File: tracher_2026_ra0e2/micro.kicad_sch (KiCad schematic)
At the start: 30 parts, among them IC1 E22-900M22S, J1 TC2030, J2 RFPC-SMA28-F, U1 R7FA0E2094CFM

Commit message: Change U1 to LQFP-48 for hand-solderable prototypes
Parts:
- U1: footprint Package_QFN:QFN-48-1EP_7x7mm_P0.5mm_EP5.6x5.6mm -> Package_QFP:LQFP-48_7x7mm_P0.5mm
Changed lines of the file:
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@@
 			)
 		)
-		(property "Footprint" "Package_QFN:QFN-48-1EP_7x7mm_P0.5mm_EP5.6x5.6mm"
+		(property "Footprint" "Package_QFP:LQFP-48_7x7mm_P0.5mm"
 			(at 180.34 97.79 0)
 			(hide yes)

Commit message: removed Acc
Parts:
- C10: value 1uF/16V -> 1uF
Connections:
- net at C10.1: no longer U1.3 (VCL)
- net MCU_I2C_SCL: no longer names the net of U1.1 (P400/SCLA1)
- net MCU_I2C_SDA: no longer names the net of U1.2 (P401/SDAA1)
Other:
- moved on the sheet: C10

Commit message: J1 Tag-Connect rewired to standard ARM 6-pin SWD pinout (1=VTRef/+3.3V, 2=SWDIO, 3=nRESET, 4=SWCLK, 5=GND, 6=NC)
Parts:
- C10: value 1uF -> 1uF/16V
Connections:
- net +3.3V: now also J1.1; no longer J1.4
- net GND: now also J1.5; no longer J1.3
- net MCU_RST: now also J1.3; no longer J1.1
- net at C10.1: now also U1.3 (VCL)
- net MCU_I2C_SCL: now reaches U1.1 (P400/SCLA1)
- net MCU_I2C_SDA: now reaches U1.2 (P401/SDAA1)
- net at U1.24 (P300/SWCLK): now also J1.4; no longer J1.6
- net at U1.25 (P108/SWDIO): now also J1.2; no longer J1.5
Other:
- moved on the sheet: C10

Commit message: Cleaned up the schamatic
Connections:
- net +3.3V: now also C11.1; no longer C11.2
- net GND: now also C11.2; no longer C11.1
- net MCU_I2C_SCL: no longer names the net of U1.1 (P400/SCLA1)
- net MCU_I2C_SDA: no longer names the net of U1.2 (P401/SDAA1)
- no-connect marks 18 -> 19
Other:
- moved on the sheet: C10, C11

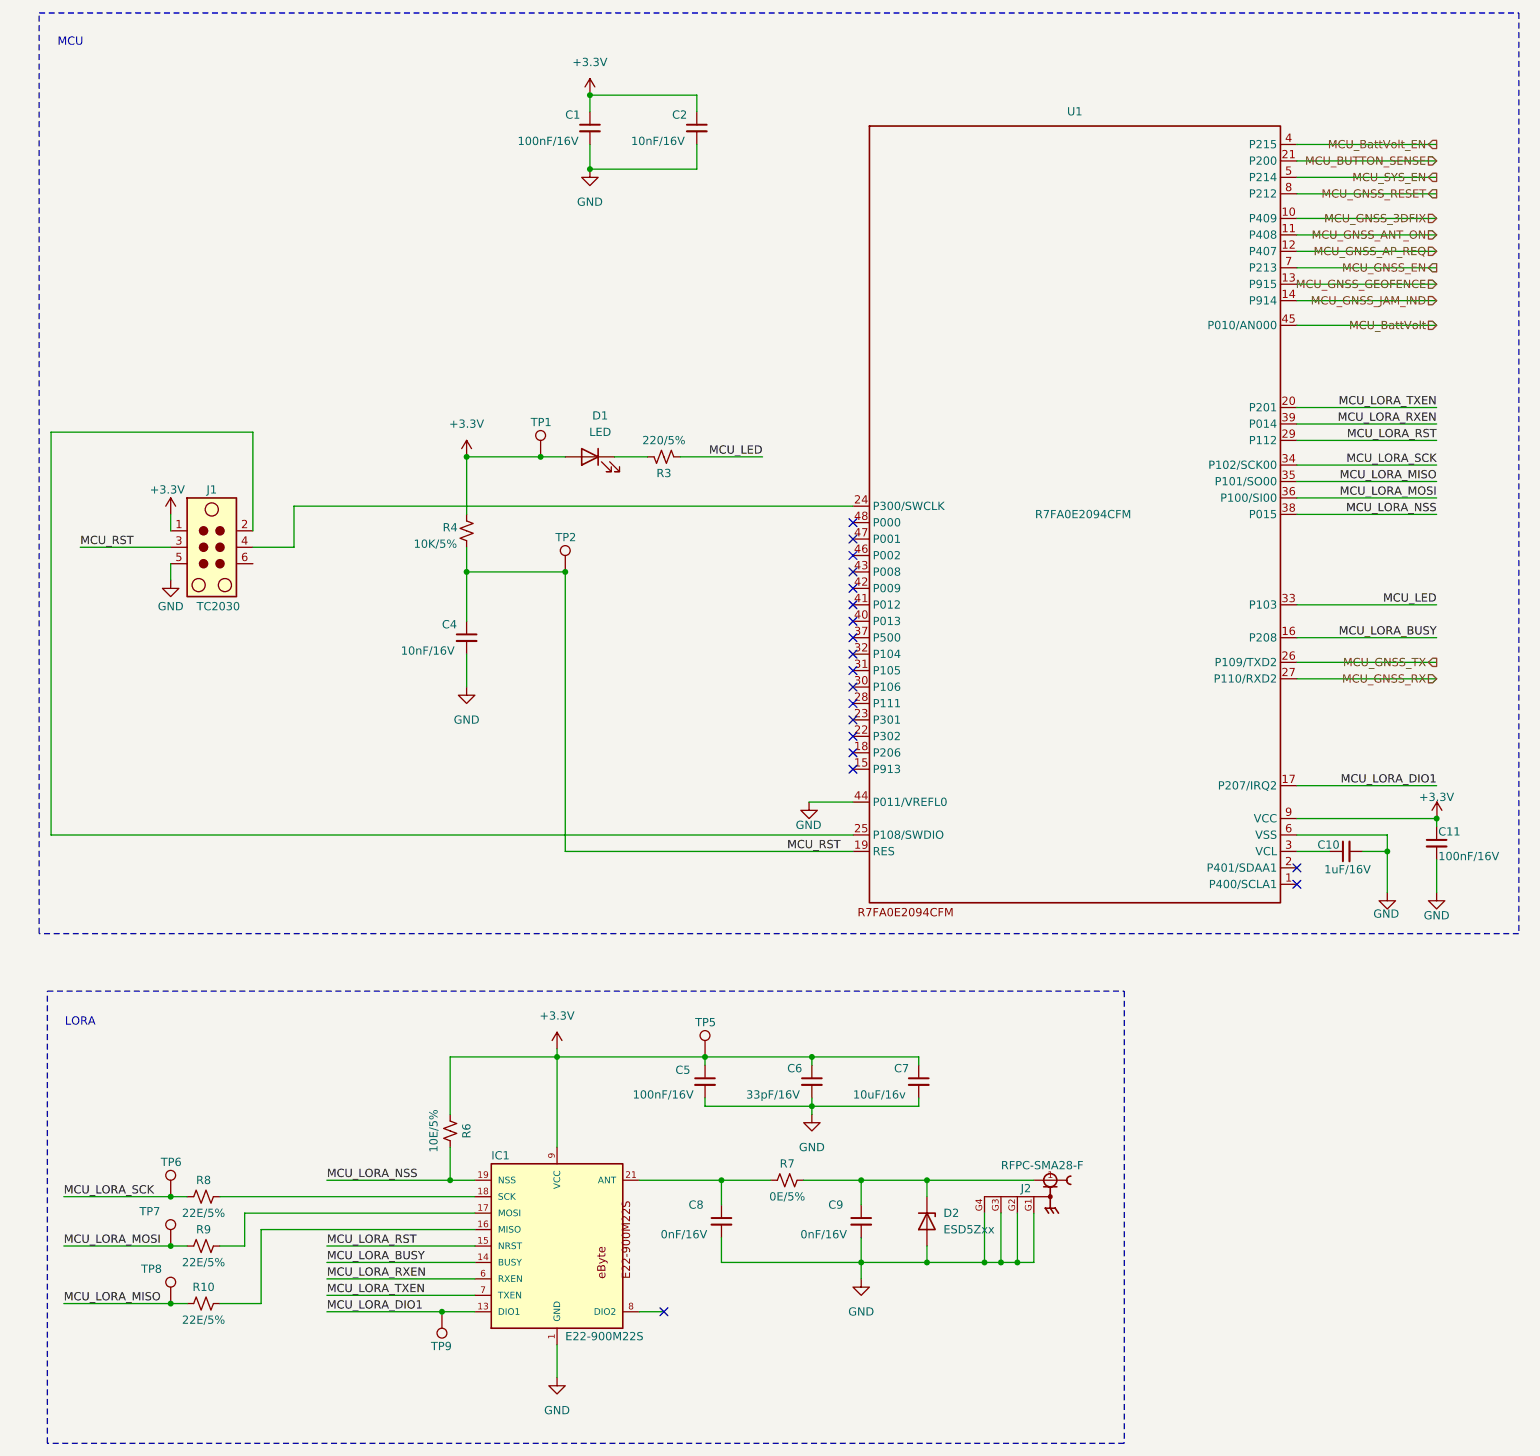
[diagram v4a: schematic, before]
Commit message: 32-pin RA0E2 (R7FA0E2094CFJ): rewrite U1 symbol and rewire schematic
- Replace 48-pin U1 with 32-pin QFN symbol (PawPrint:R7FA0E2094CFJ)
- Rewire all 23 signals per verified 32-pin assignment
- Fix P214/P215 input-only bug: BattVolt_EN->P213, SYS_EN->P212
- Remove cut nets: I2C (U5 gone), ANT_ON, AP_REQ, D_TX
- Fix J1 SWD: remove pin shorts, proper VTRef/GND, SWDIO/SWCLK via labels
- Add PawPrint.kicad_sym library and QFN-32 footprint
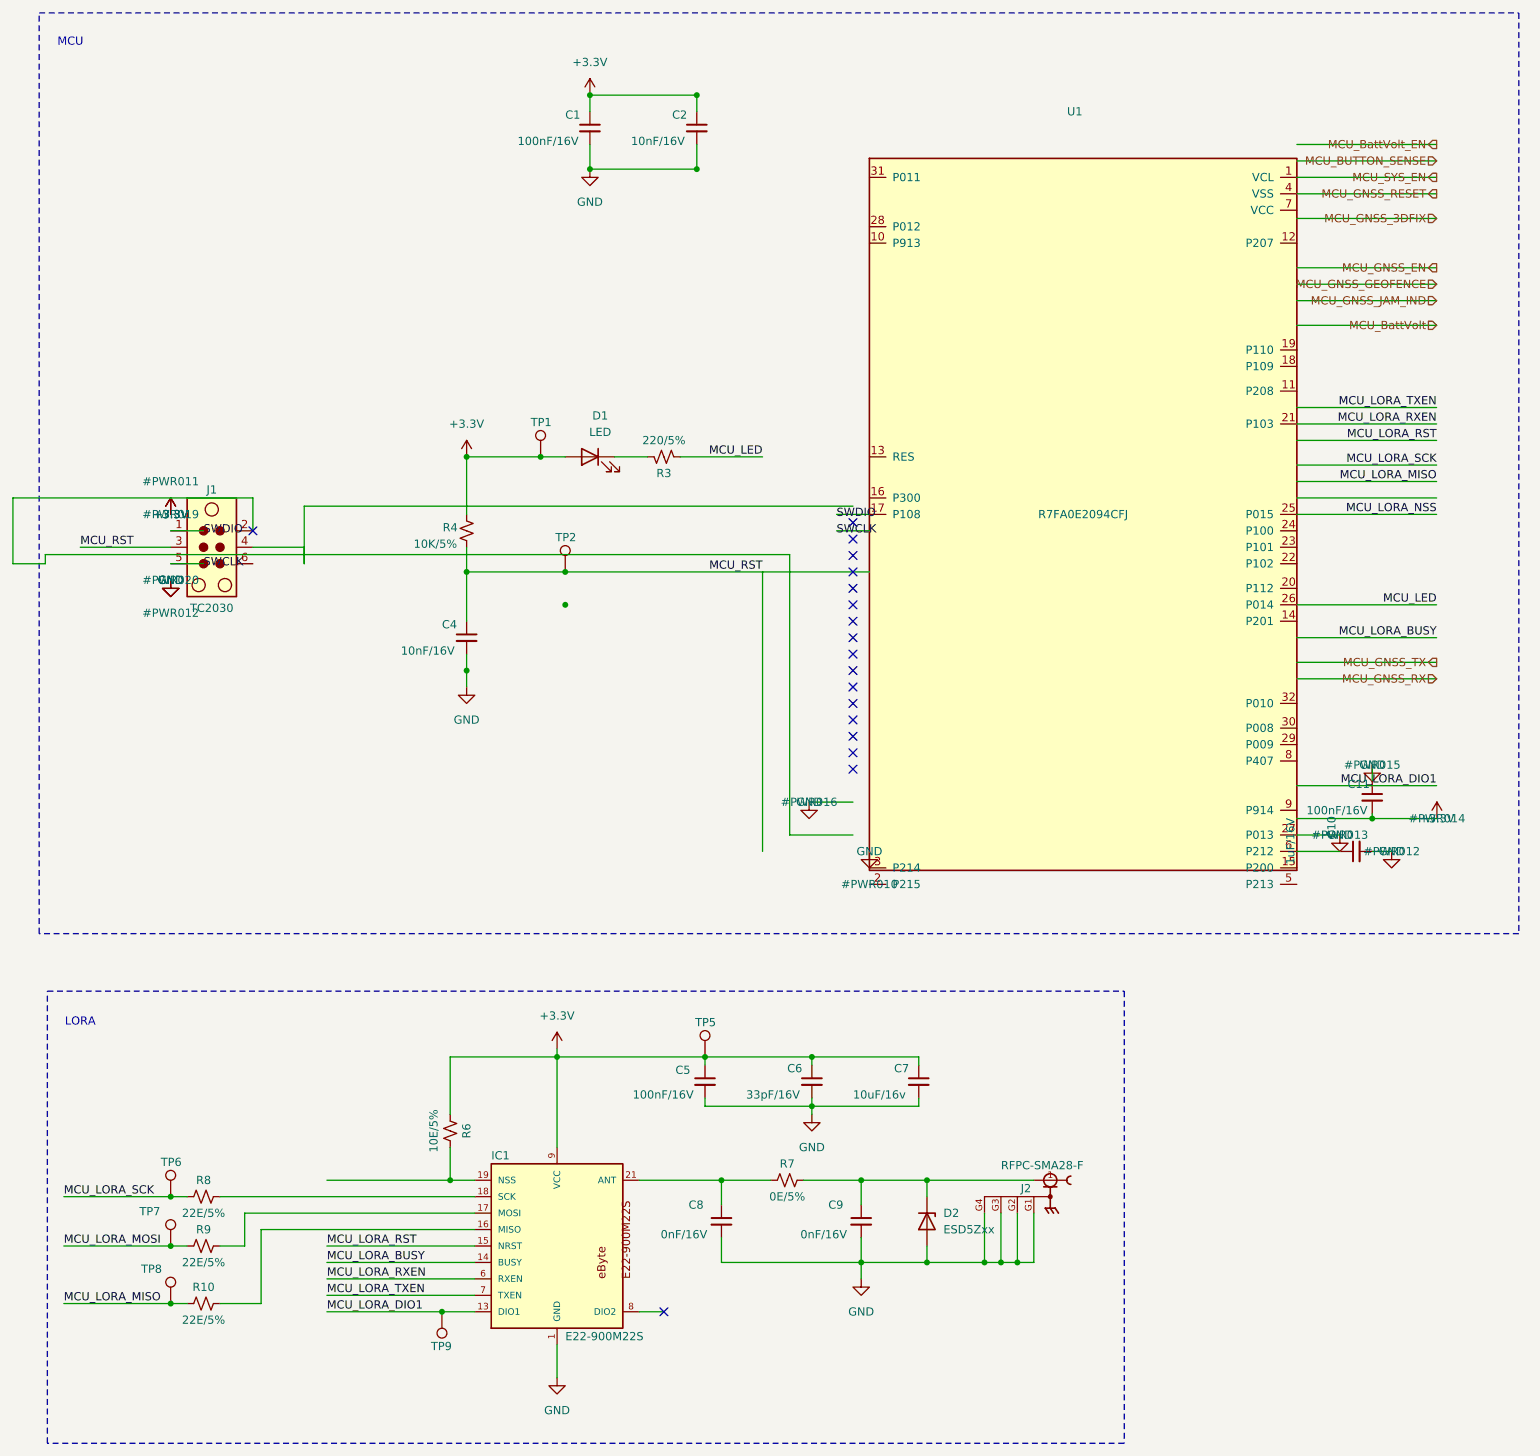
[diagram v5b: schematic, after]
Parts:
- U1: value R7FA0E2094CFM -> R7FA0E2094CFJ; footprint Package_QFP:LQFP-48_7x7mm_P0.5mm -> PawPrint:QFN-32_5x5mm_P0.5mm; symbol Custom:R7FA0E2094CFM -> PawPrint:R7FA0E2094CFJ
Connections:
- net +3.3V: now also C11.2; no longer C11.1, J1.1, U1.9 (VCC)
- net GND: now also C11.1, U1.27 (P013); no longer C11.2, J1.5, U1.44 (P011/VREFL0), U1.6 (VSS)
- net MCU_BUTTON_SENSE: no longer U1.21 (P200)
- net MCU_BattVolt: no longer U1.45 (P010/AN000)
- net MCU_BattVolt_EN: no longer U1.4 (P215)
- net MCU_GNSS_3DFIX: no longer U1.10 (P409)
- net MCU_GNSS_EN: no longer U1.7 (P213)
- net MCU_GNSS_GEOFENCE: no longer U1.13 (P915)
- net MCU_GNSS_JAM_IND: no longer U1.14 (P914)
- net MCU_GNSS_RESET: now also U1.4 (VSS); no longer U1.8 (P212)
- net MCU_GNSS_RX: no longer U1.27 (P110/RXD2)
- net MCU_GNSS_TX: no longer U1.26 (P109/TXD2)
- net MCU_LED: now also U1.26 (P014); no longer U1.33 (P103)
- net MCU_LORA_BUSY: no longer U1.16 (P208)
- net MCU_LORA_DIO1: no longer U1.17 (P207/IRQ2)
- net MCU_LORA_MISO: no longer U1.35 (P101/SO00)
- net MCU_LORA_MOSI: no longer U1.36 (P100/SI00)
- net MCU_LORA_NSS: now also U1.25 (P015); no longer IC1.19 (NSS), R6.1, U1.38 (P015)
- net MCU_LORA_RST: no longer U1.29 (P112)
- net MCU_LORA_RXEN: now also U1.21 (P103); no longer U1.39 (P014)
- net MCU_LORA_SCK: no longer U1.34 (P102/SCK00)
- net MCU_LORA_TXEN: no longer U1.20 (P201)
- net MCU_RST: no longer U1.19 (RES)
- net MCU_SYS_EN: now also U1.1 (VCL); no longer U1.5 (P214)
- net at C10.1: now also U1.6 (P212); no longer U1.3 (VCL)
- net at U1.24 (P100): no longer J1.4
- net at J1.2: no longer U1.25 (P108/SWDIO)
- net MCU_GNSS_ANT_ON: no longer names the net of U1.11 (P208)
- net MCU_GNSS_AP_REQ: no longer names the net of U1.12 (P207)
- new net: IC1.19 (NSS), R6.1
- new net SWCLK: J1.5
- new net SWDIO: J1.1, U1.17 (P108)
- no-connect marks 19 -> 18
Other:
- moved on the sheet: C10, C11
